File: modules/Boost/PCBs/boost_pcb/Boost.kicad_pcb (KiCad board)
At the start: 2 copper layers, 20 x 100 mm, 29 parts, among them J1 2x5 IDC, J2 THONKICONN, J3 THONKICONN, Q1 2N3904, U1 TL074

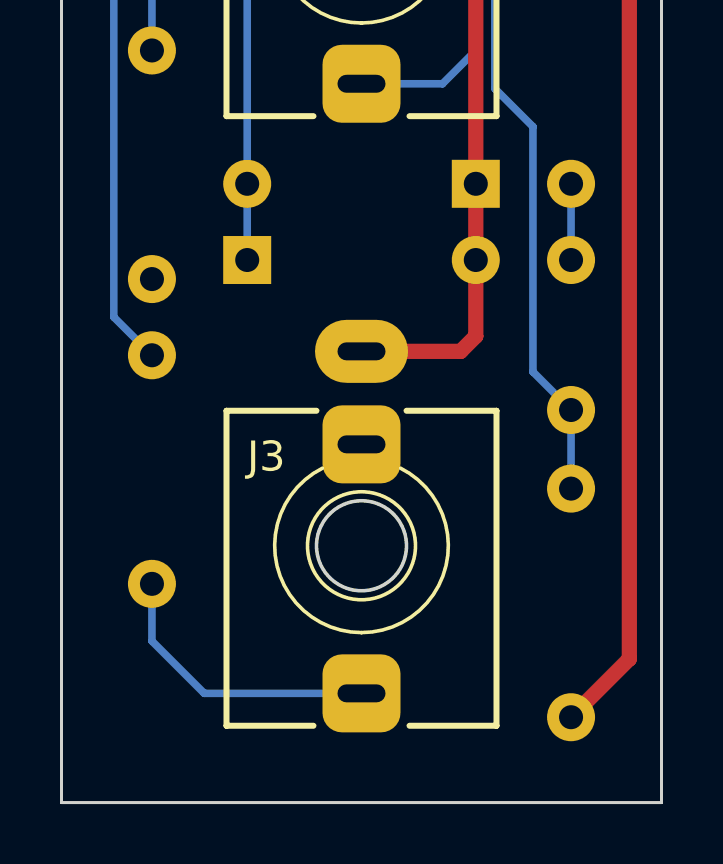
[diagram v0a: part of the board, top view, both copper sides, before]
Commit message: Fix Boost jack socket alignment
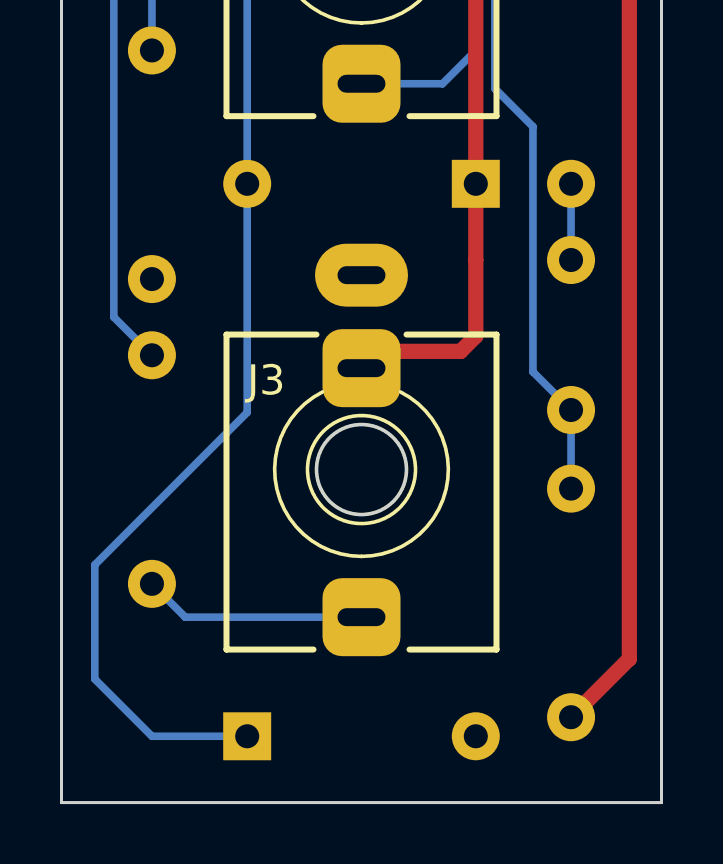
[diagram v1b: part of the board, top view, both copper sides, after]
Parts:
- C2: value 1uF -> 10nF
- moved D2 15.9 mm to (31.8, 123.2)
- moved J3 2.54 mm to (35.6, 114.3)
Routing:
- net Net-(D1-A): track 30.0 -> 52.0 mm
- net Net-(J3-Pad3): track 9.61 -> 7.44 mm
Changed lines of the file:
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@@
 	(footprint "FreeModular:THONKICONN"
 		(layer "F.Cu")
-		(at 35.56 116.84 180)
+		(at 35.56 114.3 180)
 		(property "Reference" "J3"
 			(at 3.175 2.97 0)
@@
 		)
 		(fp_text user "${REFERENCE}"
-			(at 4.5 -9.5 0)
+			(at 3.175 3.175 0)
 			(layer "F.Fab")
 			(effects
@@
 			)
 		)
-		(property "Value" "1uF"
+		(property "Value" "10nF"
 			(at 2.5 -2.5 0)
 			(layer "B.Fab")
@@
 	(footprint "Diode_THT:D_DO-35_SOD27_P7.62mm_Horizontal"
 		(layer "B.Cu")
-		(at 31.75 107.315)
+		(at 31.75 123.19)
 		(descr "Diode, DO-35_SOD27 series, Axial, Horizontal, pin pitch=7.62mm, , length*diameter=4*2mm^2, , http://www.diodes.com/_files/packages/DO-35.pdf")
 		(tags "Diode DO-35_SOD27 series Axial Horizontal pin pitch 7.62mm  length 4mm diameter 2mm")
@@
 		)
 		(fp_text user "K"
-			(at 0 1.8 0)
+			(at 0 -1.905 180)
 			(layer "B.SilkS")
 			(effects
@@
 	)
 	(segment
-		(start 28.575 120.015)
-		(end 28.575 118.11)
-		(width 0.254)
-		(layer "B.Cu")
-		(net 2)
-	)
-	(segment
-		(start 30.32 121.76)
-		(end 28.575 120.015)
+		(start 35.56 119.22)
+		(end 29.685 119.22)
 		(width 0.254)
 		(layer "B.Cu")
@@
 	)
 	(segment
-		(start 35.56 121.76)
-		(end 30.32 121.76)
+		(start 29.685 119.22)
+		(end 28.575 118.11)
 		(width 0.254)
 		(layer "B.Cu")
@@
 	)
 	(segment
+		(start 31.75 112.395)
+		(end 26.67 117.475)
+		(width 0.254)
+		(layer "B.Cu")
+		(net 6)
+	)
+	(segment
 		(start 31.75 104.775)
 		(end 31.75 87.63)
@@
 	)
 	(segment
+		(start 28.575 123.19)
+		(end 31.75 123.19)
+		(width 0.254)
+		(layer "B.Cu")
+		(net 6)
+	)
+	(segment
+		(start 31.75 104.775)
+		(end 31.75 112.395)
+		(width 0.254)
+		(layer "B.Cu")
+		(net 6)
+	)
+	(segment
 		(start 31.115 84.455842)
 		(end 33.02 82.550842)
@@
 	)
 	(segment
-		(start 31.75 104.775)
-		(end 31.75 107.315)
+		(start 26.67 117.475)
+		(end 26.67 121.285)
+		(width 0.254)
+		(layer "B.Cu")
+		(net 6)
+	)
+	(segment
+		(start 26.67 121.285)
+		(end 28.575 123.19)
 		(width 0.254)
 		(layer "B.Cu")

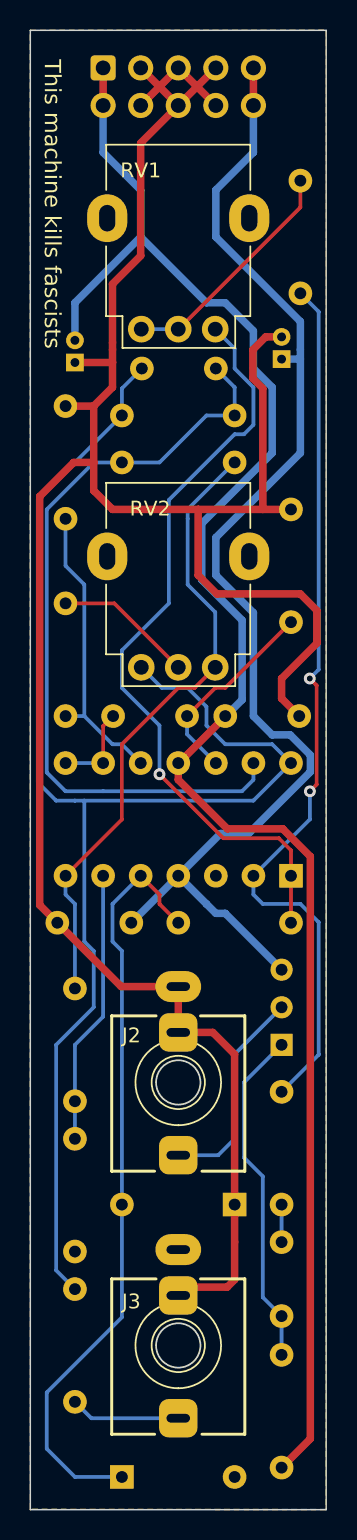
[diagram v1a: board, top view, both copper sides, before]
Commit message: Flip boost pots
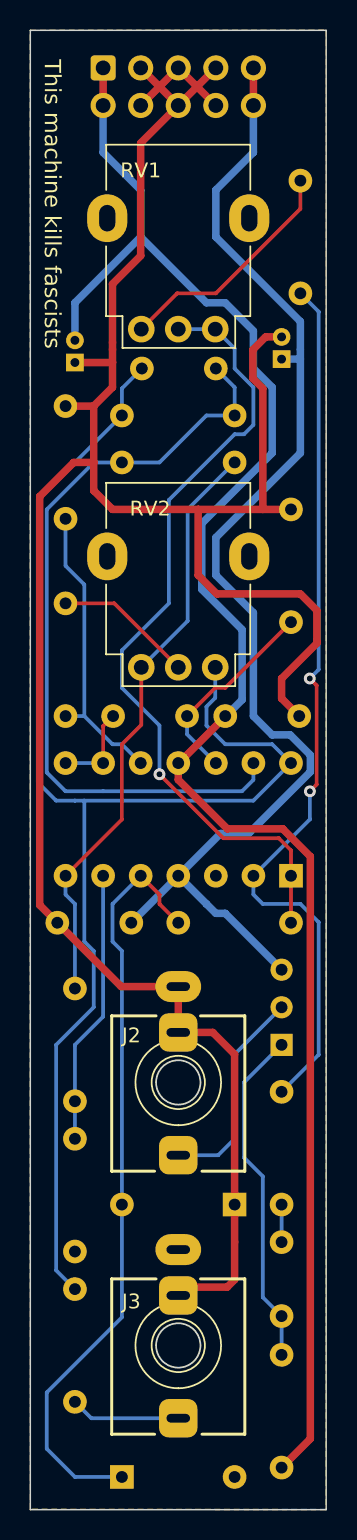
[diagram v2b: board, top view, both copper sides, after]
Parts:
- removed REF**: logo_very_small, FreeModular:logo_very_small
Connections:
- RV1 pad 2: Net-(R3-Pad2) -> Net-(R4-Pad1)
- RV2 pad 1: Net-(C3-Pad2) -> Net-(R10-Pad2)
- RV2 pad 3: Net-(R10-Pad2) -> Net-(C3-Pad2)
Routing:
- net Net-(C3-Pad2): track 98.0 -> 95.4 mm
- net Net-(R4-Pad1): track 52.2 -> 54.7 mm
- net Net-(R10-Pad2): track 42.8 -> 40.6 mm
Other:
- board text added: "Free Modular Boost v1.1"
- board text removed: "Free Modular Boost v1.0"
